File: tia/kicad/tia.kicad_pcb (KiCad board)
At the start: 2 copper layers, 22 x 22 mm, 26 parts, among them J1 SSQ-103-01-G-D, P1 73415-2061, U1 OPA847IDBVT, U2 OPA843IDBVT

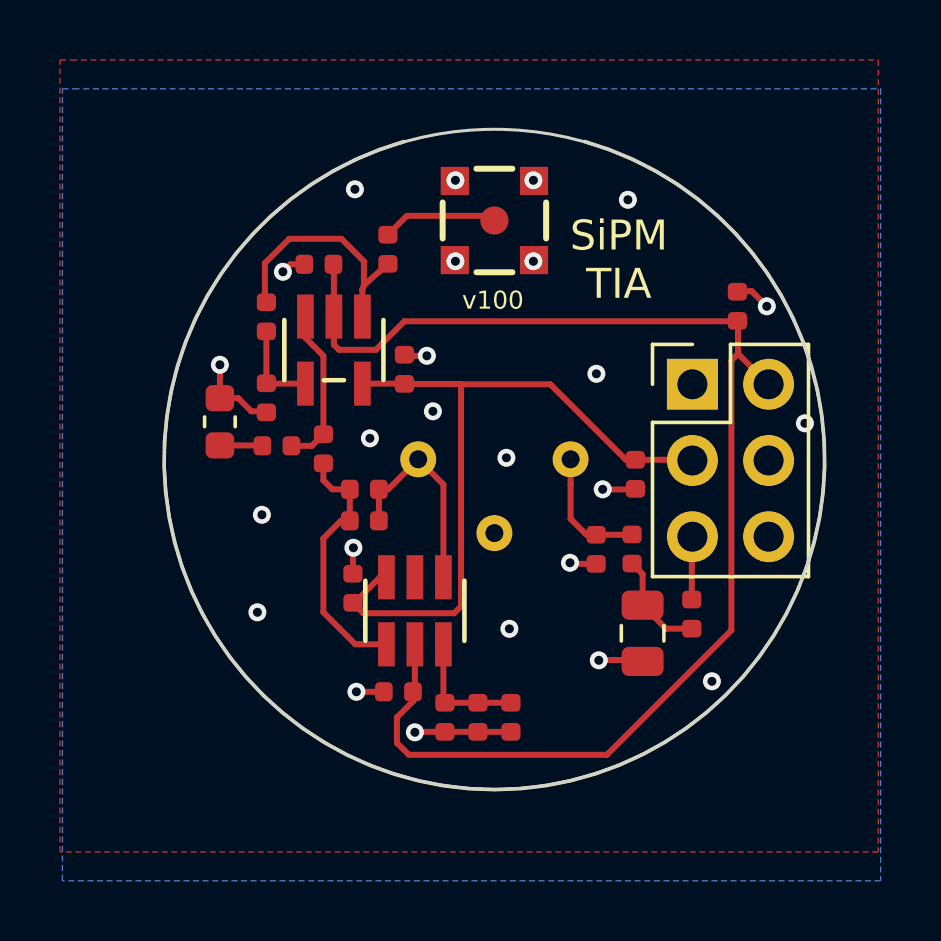
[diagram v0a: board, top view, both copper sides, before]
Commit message: fix sipm footprint
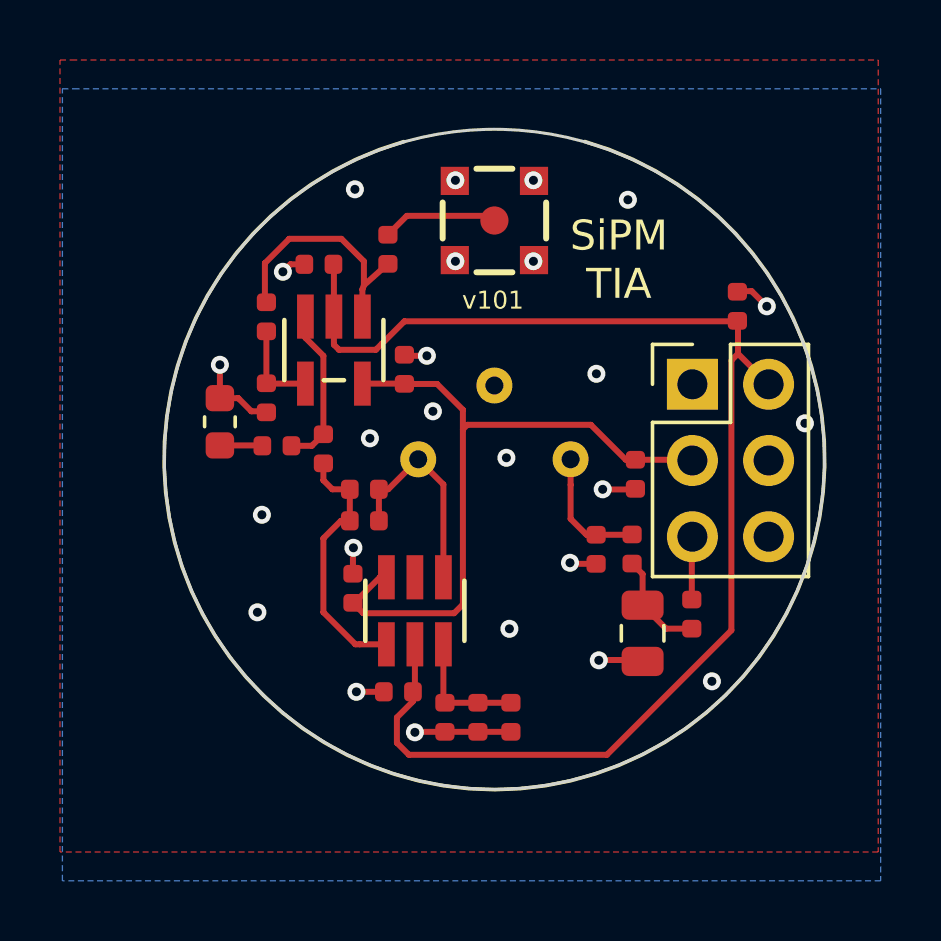
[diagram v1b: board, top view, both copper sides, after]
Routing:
- net VDDA: track 25.4 -> 24.4 mm
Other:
- board text added: "v101"
- board text removed: "v100"
